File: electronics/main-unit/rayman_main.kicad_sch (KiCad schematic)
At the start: 108 parts, among them M1 M1, M2 M2, Q1 BC817, T1A_FUSE2 1808 SMD FUSEHOLDER, U1 ESP32-S3-WROOM-1, U2 SN74AHCT125N, U3 MCP1826S-3302E/DB, U4 SSR-DA41F

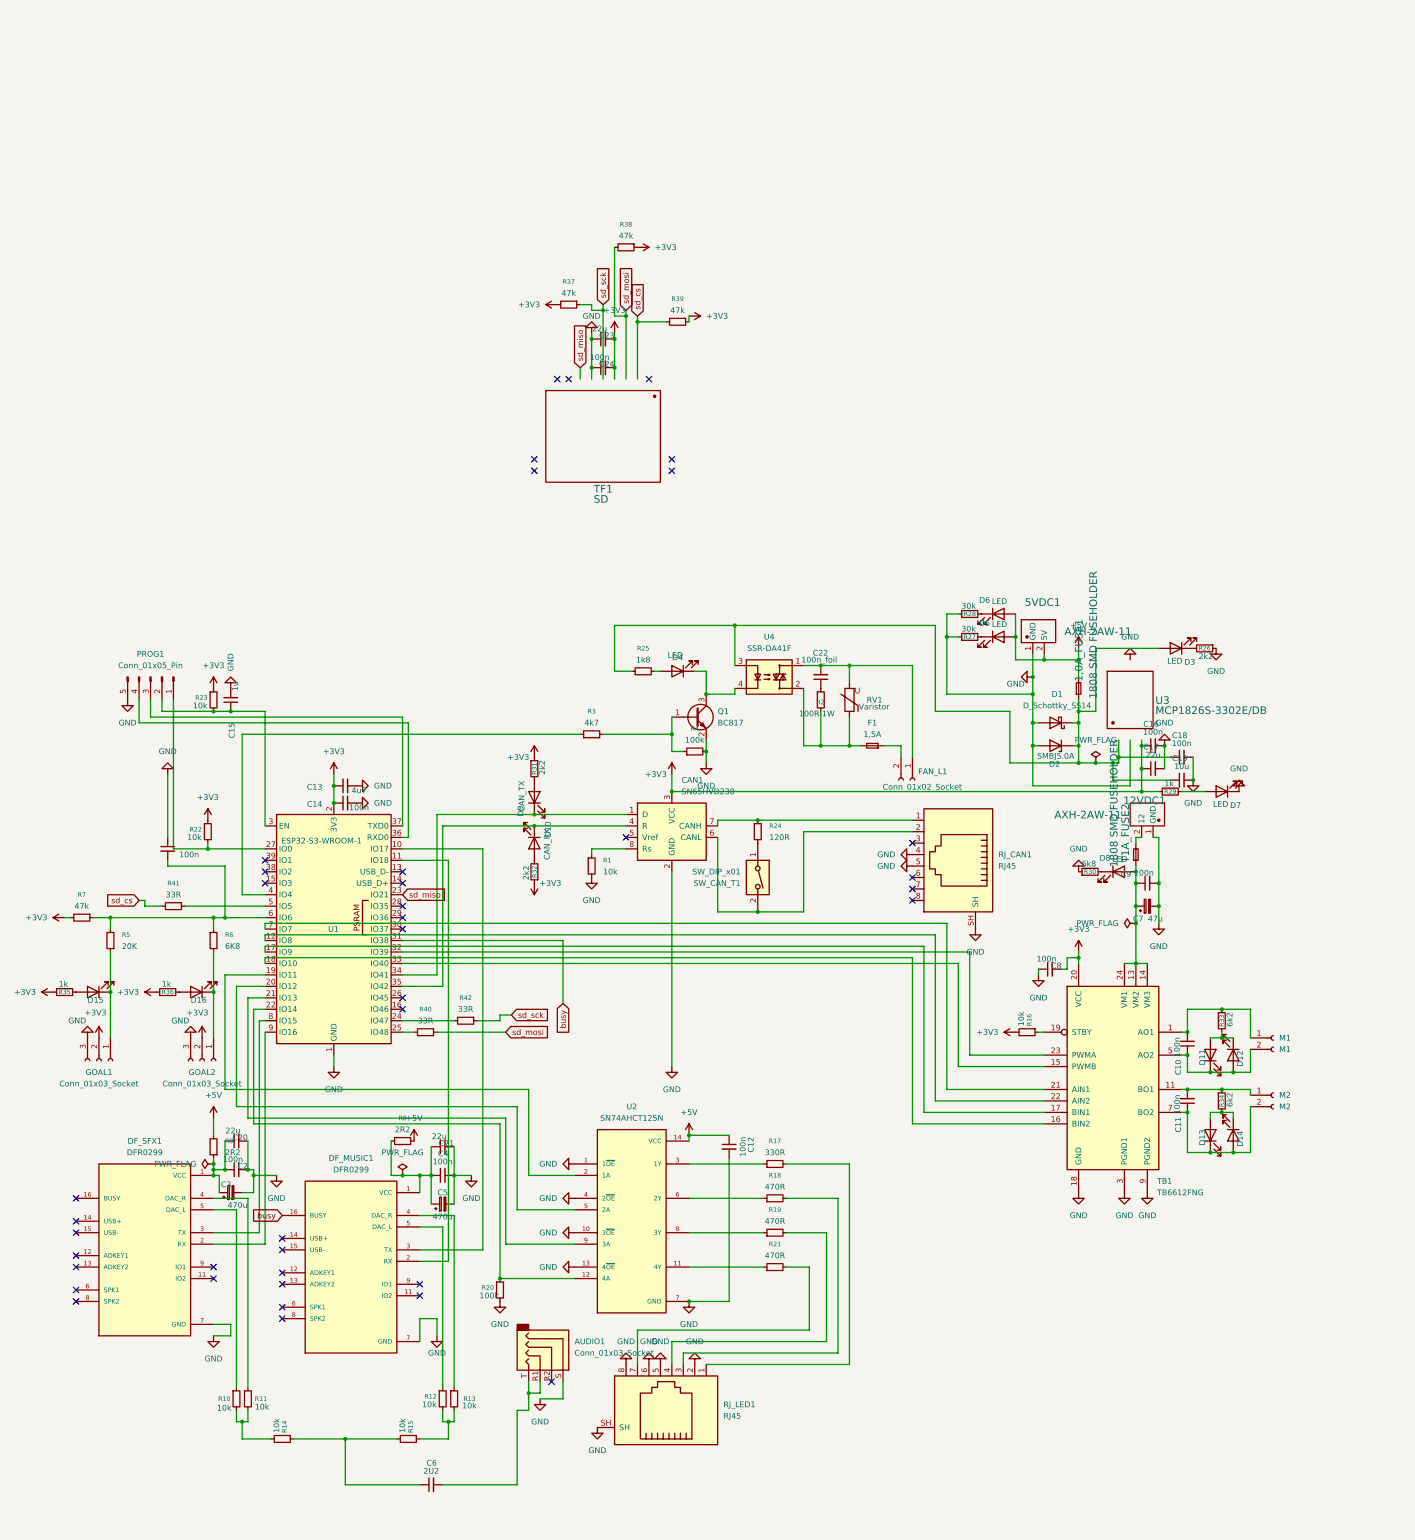
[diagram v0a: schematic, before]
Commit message: lamp animation fix
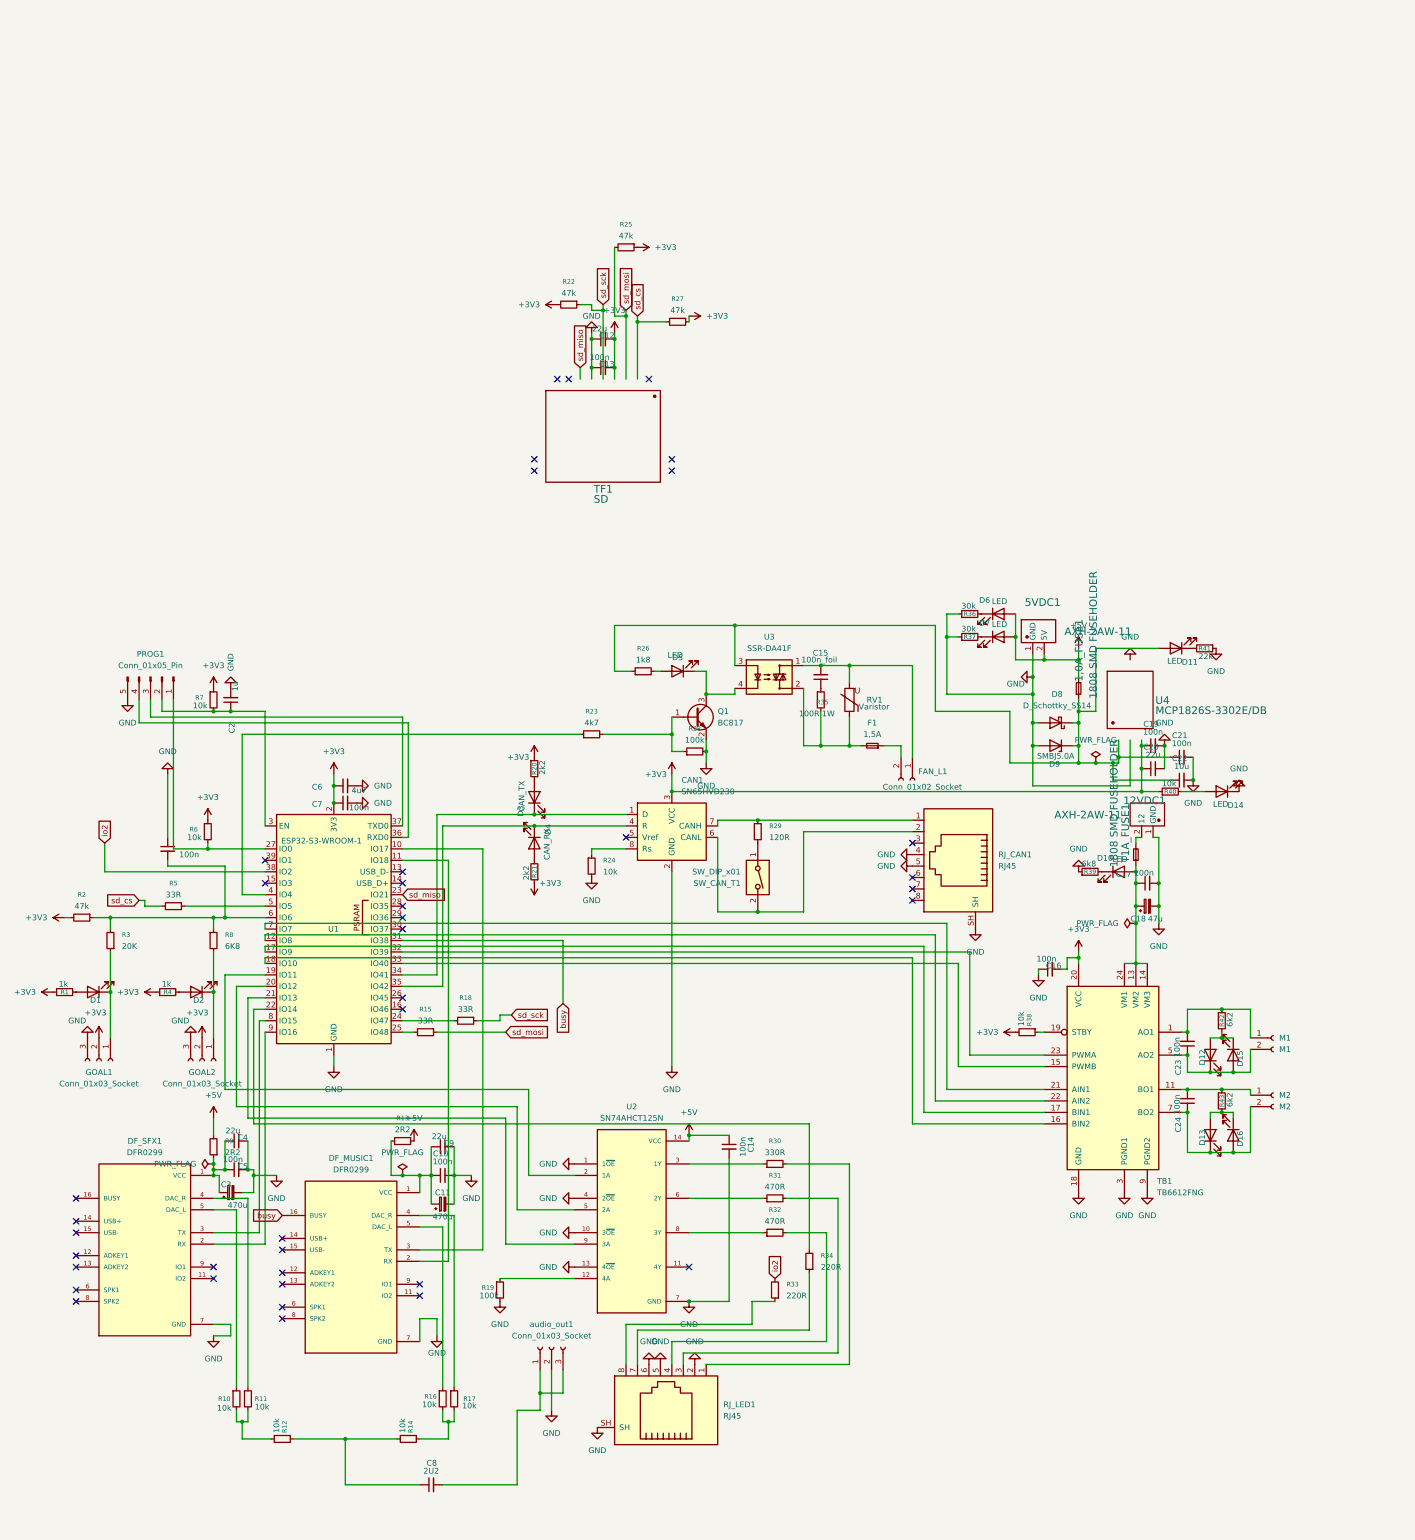
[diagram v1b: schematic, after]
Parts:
- removed AUDIO1: Conn_01x03_Socket, Connector_Audio:Jack_3.5mm_PJ320D_Horizontal, symbol Connector_Audio:AudioJack4
- removed R21: 470R, Resistor_SMD:R_0805_2012Metric, symbol Device:R_Small
- added R33, R34: 220R, Resistor_SMD:R_0805_2012Metric, symbol Device:R_Small
- added audio_out1: Conn_01x03_Socket, Connector_JST:JST_PH_B3B-PH-SM4-TB_1x03-1MP_P2.00mm_Vertical, symbol Connector:Conn_01x03_Socket
- R40: renamed from R29; value 1k -> 10k
- R41: renamed from R26; value 2k2 -> 22k
- renumbered C4 to C10, C5 to C11, C23 to C12, C24 to C13, C12 to C14, C22 to C15, C8 to C16, C9 to C17, C7 to C18, C16 to C19, C15 to C2, C17 to C20, C18 to C21, C19 to C22, C10 to C23, C11 to C24, C20 to C4, C2 to C5, C13 to C6, C14 to C7, C6 to C8, C21 to C9, D15 to D1, D8 to D10, D3 to D11, D11 to D12, D7 to D14, D12 to D15, D14 to D16, D16 to D2, D9 to D3, D10 to D4, D4 to D5, D5 to D7, D1 to D8, D2 to D9, R35 to R1, R14 to R12, R8 to R13, R15 to R14, R40 to R15, R12 to R16, R13 to R17, R42 to R18, R20 to R19, R7 to R2, R31 to R20, R32 to R21, R37 to R22, R3 to R23, R1 to R24, R38 to R25, R25 to R26, R39 to R27, R4 to R28, R24 to R29, R5 to R3, R17 to R30, R18 to R31, R19 to R32, R2 to R35, R28 to R36, R27 to R37, R16 to R38, R30 to R39, R36 to R4, R33 to R42, R34 to R43, R41 to R5, R22 to R6, R23 to R7, R6 to R8, T1A_FUSE2 to T1A_FUSE1, U4 to U3, U3 to U4
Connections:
- net GND: now also audio_out1.2 (VCC); no longer RJ_LED1.8
- net at R19.1, U2.12 (4A): no longer U1.22 (IO14)
- net at C8.2: now also audio_out1.1 (DO), audio_out1.3 (GND)
- net at RJ_LED1.7: now also R34.1
- net io2: now reaches U1.38 (IO2)
- net io2: now also R33.2
- new net: R34.2, U1.22 (IO14)
- new net: R33.1, RJ_LED1.8
- no-connect marks 40 -> 39

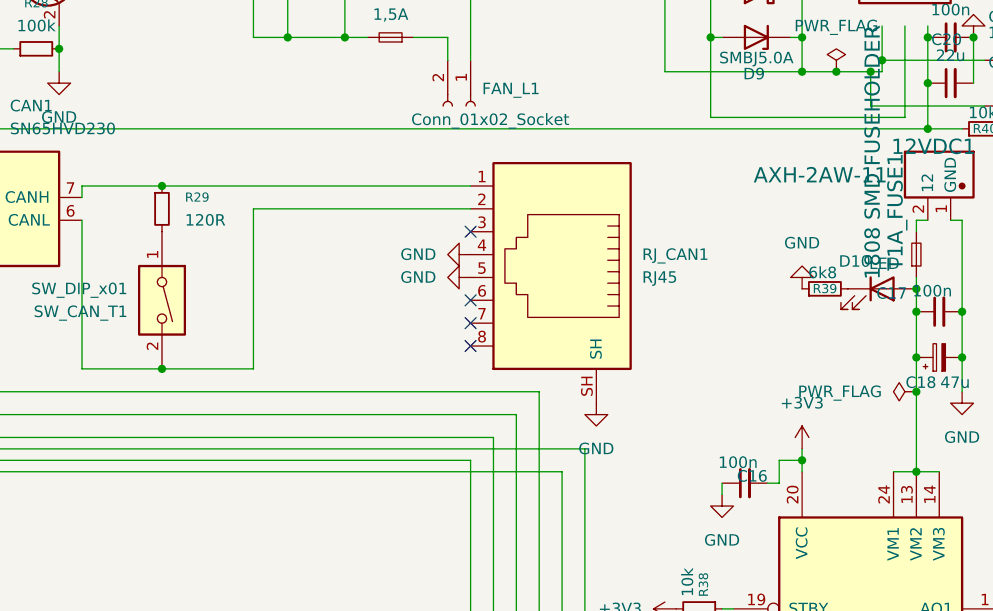
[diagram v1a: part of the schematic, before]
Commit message: lamp fans control added; uv boost anims added; ambiente light timeout fixed
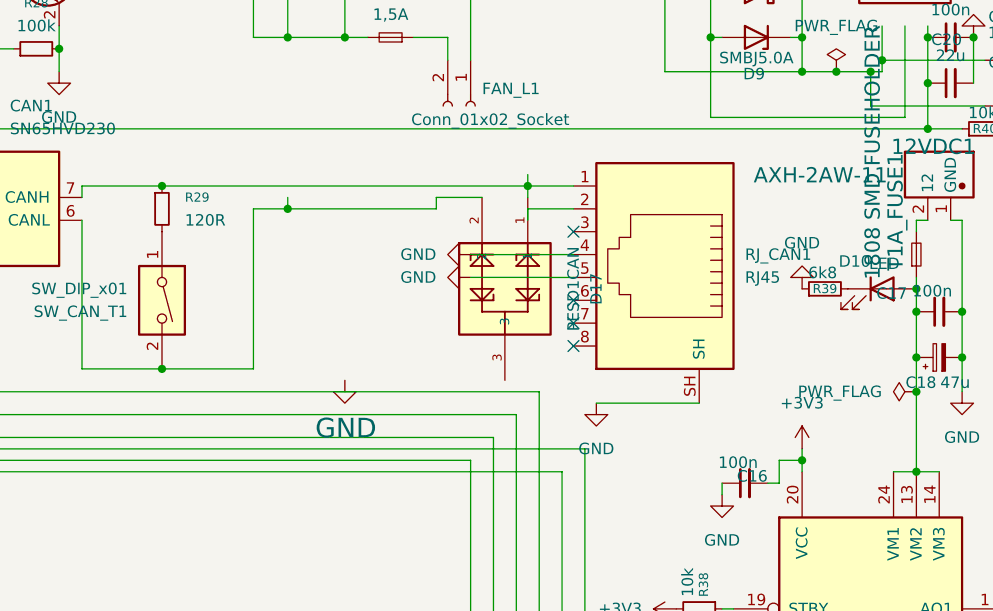
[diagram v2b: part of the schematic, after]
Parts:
- added D17: PESD1CAN, moja:SOT23-3, symbol moja:PESD1CAN
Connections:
- net at CAN1.6 (CANL), SW_CAN_T1.2: now also D17.2; no longer RJ_CAN1.2
- net at CAN1.7 (CANH), R29.1, RJ_CAN1.1: now also D17.1
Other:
- moved on the sheet: RJ_CAN1

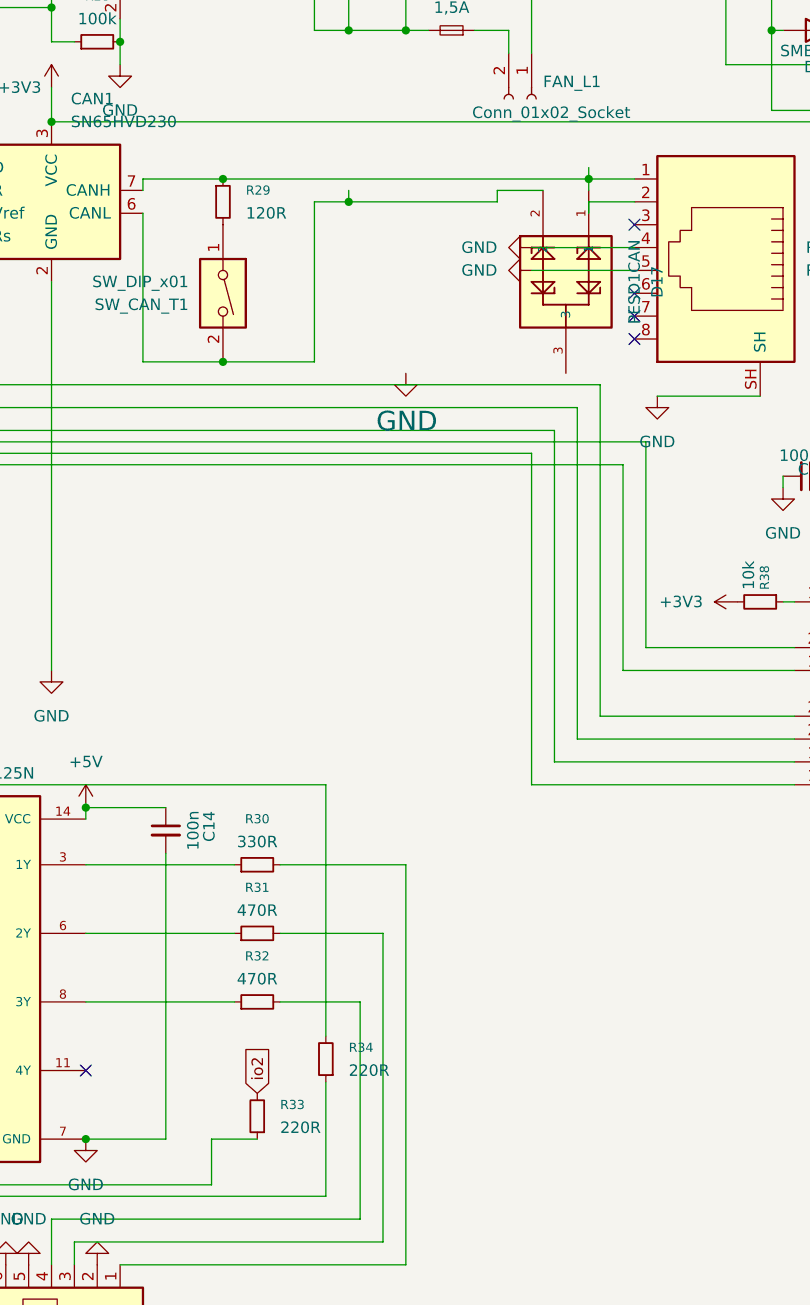
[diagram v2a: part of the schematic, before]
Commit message: fail safe added to lamp fans
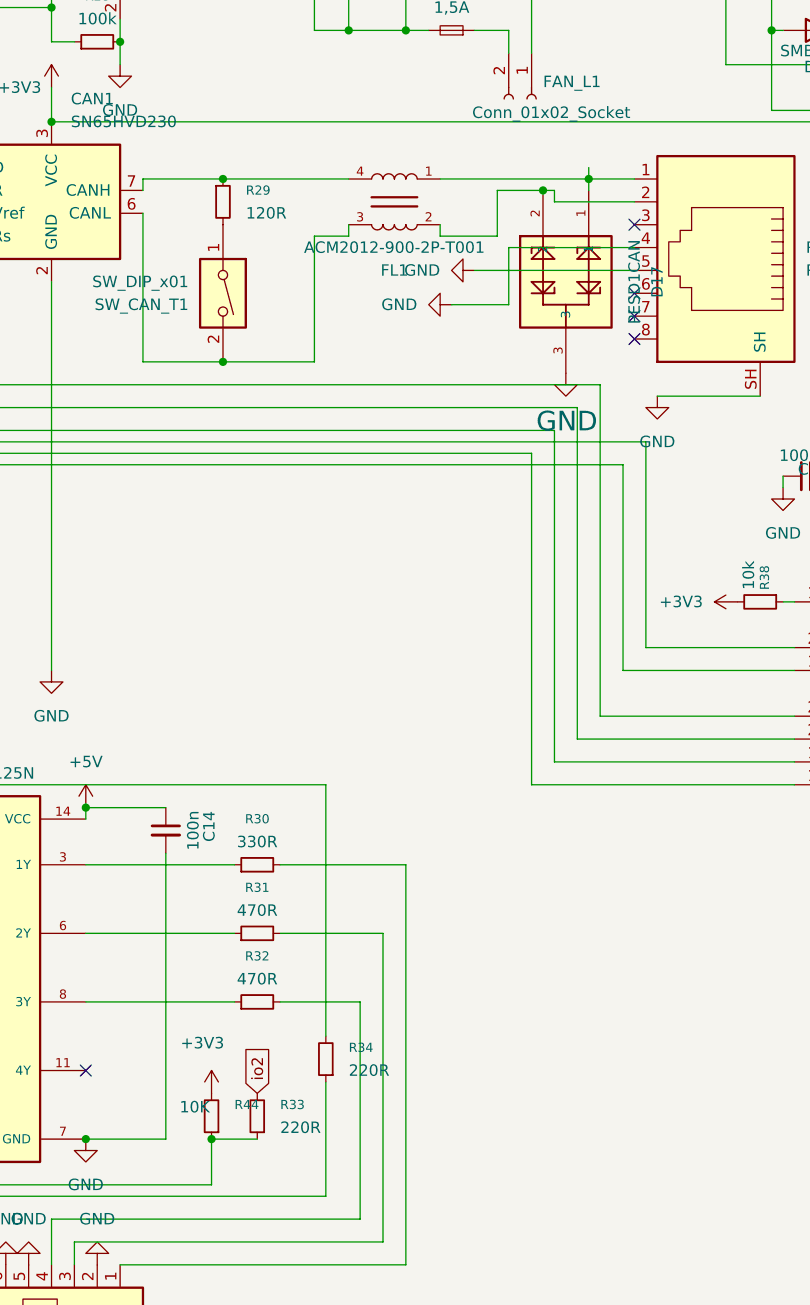
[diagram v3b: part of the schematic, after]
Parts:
- added FL1: ACM2012-900-2P-T001, moja:FIL_ACM2012-900-2P-T001, symbol moja:ACM2012-900-2P-T001
- added R44: 10K, Resistor_SMD:R_0805_2012Metric, symbol Device:R_Small
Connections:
- net +3V3: now also R44.2
- net at D17.1, RJ_CAN1.1: now also FL1.1; no longer CAN1.7 (CANH), R29.1
- net at CAN1.6 (CANL), SW_CAN_T1.2: now also FL1.3; no longer D17.2
- net at RJ_CAN1.2: now also D17.2, FL1.2
- net at R33.1, RJ_LED1.8: now also R44.1
- new net: CAN1.7 (CANH), FL1.4, R29.1

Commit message: uv control fixed
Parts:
- removed R19: 100k, Resistor_SMD:R_0805_2012Metric, symbol Device:R_Small
- added U5: SP3012-06UTG, moja:SON50P350X135X55-14N, symbol moja:SP3012-06UTG
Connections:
- net GND: now also U5.10, U5.5
- net io2: now also U2.12 (4A); no longer R33.2
- net sd_cs: now also U5.6, U5.9
- net sd_miso: now also U5.1, U5.14
- net sd_mosi: now also U5.11, U5.4
- net sd_sck: now also U5.12, U5.3
- net at U2.11 (4Y): now also R33.2
- no-connect marks 39 -> 42
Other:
- moved on the sheet: R22, R25

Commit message: Ambiente lighting draft, song order fixet for music rounds, many others
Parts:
- added C25: 100n, Capacitor_SMD:C_0805_2012Metric, symbol Device:C_Small
- added U6: STEF4SPUR, moja:STEF05PUR, symbol moja:STEF4SPUR
- R10, R11, R16, R17: value 10k -> 2k2
- R12: value 10k -> 100k
- R20, R21: value 2k2 -> 68R
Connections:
- net +5V: now also R26.1, U3.3, U6.10 (V_OUT), U6.8 (V_OUT), U6.9 (V_OUT); no longer 1,0A_FUSE1.2, 5VDC1.2 (5V)
- net GND: now also R12.2, C25.2, U6.11 (GND), U6.5 (GND)
- net at 1,0A_FUSE1.1, C21.1, C22.1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: no longer R26.1, U3.3
- net at R10.2, R11.2: now also C8.1, R16.2, R17.2; no longer R12.2
- net at C8.2, audio_out1.1 (DO), audio_out1.3 (GND): now also R12.1
- new net: C25.1, U6.6 (SST)
- new net: R14.2, U6.7 (EN)
- new net 5v_b4_prot: 1,0A_FUSE1.2, 5VDC1.2 (5V), R14.1, U6.1 (V_IN), U6.2 (V_IN), U6.3 (V_IN), U6.4 (V_CP)
- no-connect marks 42 -> 39
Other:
- moved on the sheet: U4
